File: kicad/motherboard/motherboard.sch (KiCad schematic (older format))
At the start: 21 parts, among them J1 DB37_Female, J10 DB37_Female, J11 DB37_Female, J12 Barrel_Jack, J13 TSR 1-2433, J2 DB37_Female, J3 DB37_Female, J4 DB37_Female, J5 DB37_Female, J6 DB25_Female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

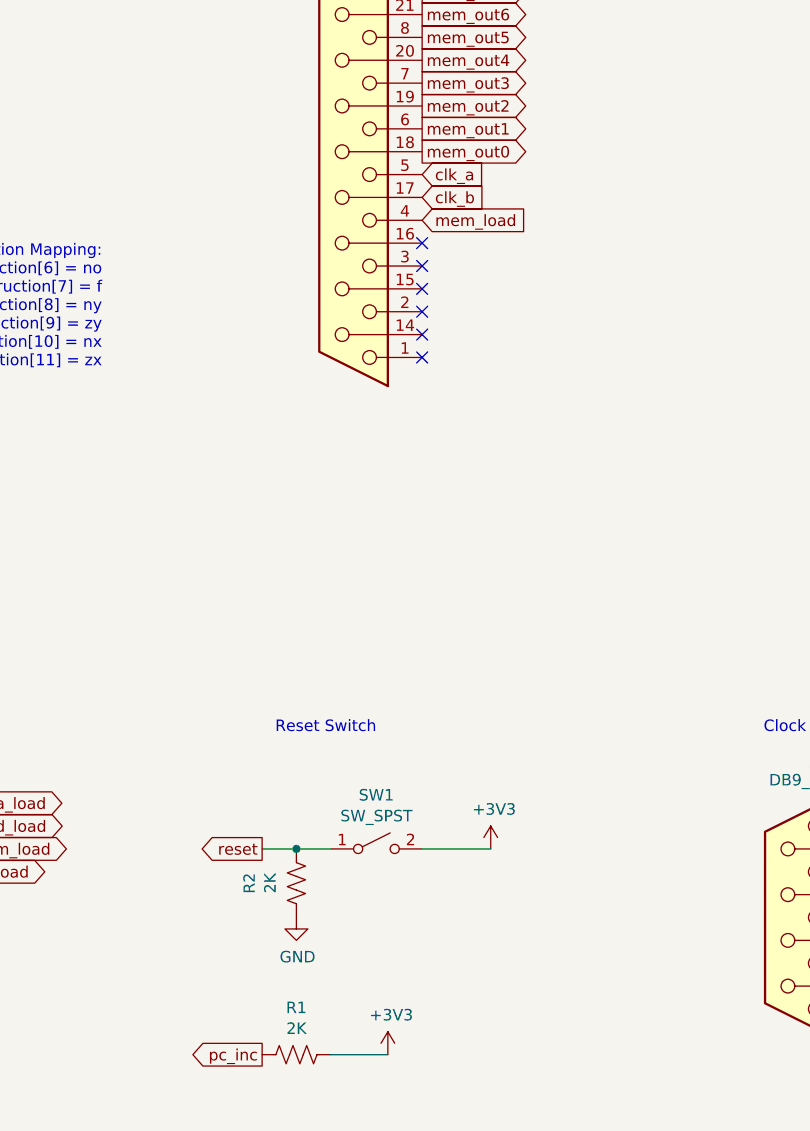
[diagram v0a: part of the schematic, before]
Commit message: Motherboard fully routed, PCB layout done
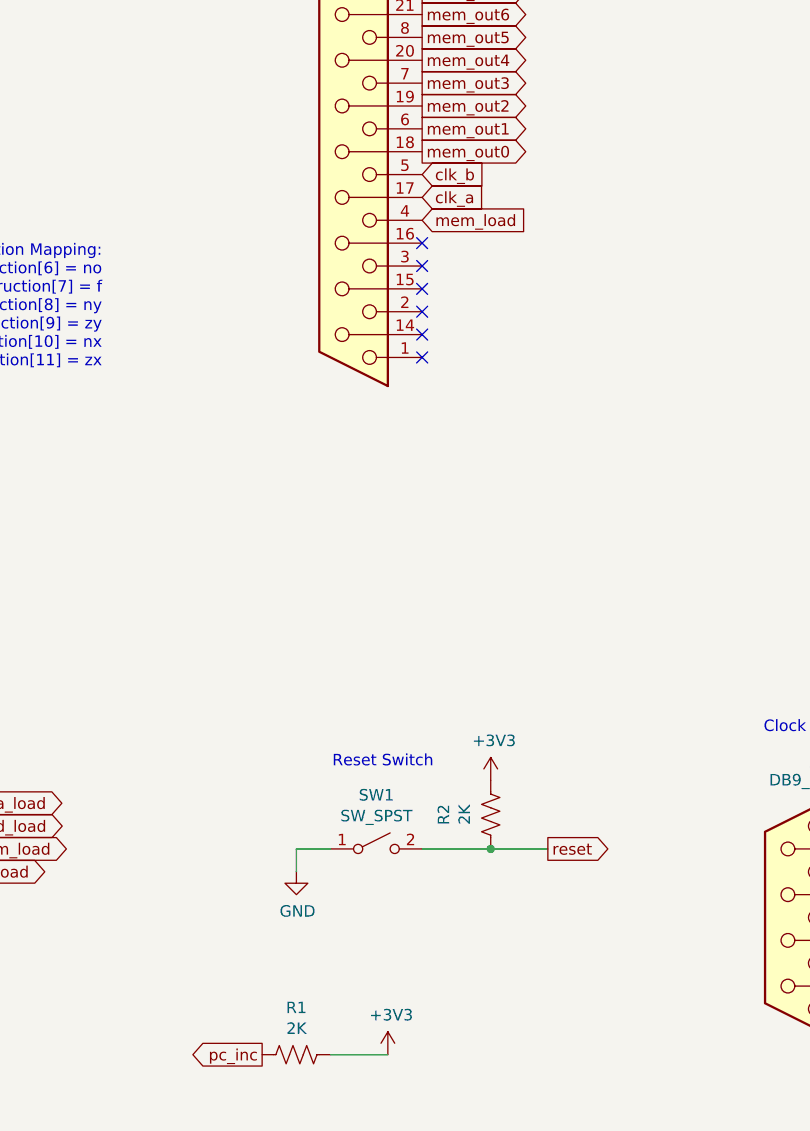
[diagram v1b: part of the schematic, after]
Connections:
- net +3V3: now also R2.1; no longer SW1.2 (B)
- net GND: now also SW1.1 (A); no longer R2.2
- net clk_a: now also J8.17 (P17); no longer J8.5
- net clk_b: now also J8.5; no longer J8.17 (P17)
- net reset: now also R2.2, SW1.2 (B); no longer R2.1, SW1.1 (A)
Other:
- moved on the sheet: R2
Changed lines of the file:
@@
 	1    0    0    -1
 $EndComp
-Text GLabel 3850 9800 0    50   Output ~ 0
+Text GLabel 5100 9800 2    50   Output ~ 0
 reset
 $Comp
 L Device:R_US R2
 U 1 1 5EA8D68F
-P 4000 9950
-F 0 "R2" V 3795 9950 50  0000 C CNN
-F 1 "2K" V 3886 9950 50  0000 C CNN
-F 2 "Resistor_SMD:R_1206_3216Metric" V 4040 9940 50  0001 C CNN
-F 3 "~" H 4000 9950 50  0001 C CNN
-	1    4000 9950
+P 4850 9650
+F 0 "R2" V 4645 9650 50  0000 C CNN
+F 1 "2K" V 4736 9650 50  0000 C CNN
+F 2 "Resistor_SMD:R_1206_3216Metric" V 4890 9640 50  0001 C CNN
+F 3 "~" H 4850 9650 50  0001 C CNN
+	1    4850 9650
 	1    0    0    -1
 $EndComp
@@
 L power:GND #PWR054
 U 1 1 5EA903DA
-P 4000 10100
-F 0 "#PWR054" H 4000 9850 50  0001 C CNN
-F 1 "GND" H 4005 9927 50  0000 C CNN
-F 2 "" H 4000 10100 50  0001 C CNN
-F 3 "" H 4000 10100 50  0001 C CNN
-	1    4000 10100
+P 4000 9900
+F 0 "#PWR054" H 4000 9650 50  0001 C CNN
+F 1 "GND" H 4005 9727 50  0000 C CNN
+F 2 "" H 4000 9900 50  0001 C CNN
+F 3 "" H 4000 9900 50  0001 C CNN
+	1    4000 9900
 	1    0    0    -1
 $EndComp
@@
 L power:+3V3 #PWR053
 U 1 1 5EA90EB0
-P 4850 9800
-F 0 "#PWR053" H 4850 9650 50  0001 C CNN
-F 1 "+3V3" H 4865 9973 50  0000 C CNN
-F 2 "" H 4850 9800 50  0001 C CNN
-F 3 "" H 4850 9800 50  0001 C CNN
-	1    4850 9800
-	1    0    0    -1
-$EndComp
-Wire Wire Line
-	3850 9800 4000 9800
-Connection ~ 4000 9800
+P 4850 9500
+F 0 "#PWR053" H 4850 9350 50  0001 C CNN
+F 1 "+3V3" H 4865 9673 50  0000 C CNN
+F 2 "" H 4850 9500 50  0001 C CNN
+F 3 "" H 4850 9500 50  0001 C CNN
+	1    4850 9500
+	1    0    0    -1
+$EndComp
 Wire Wire Line
 	4000 9800 4150 9800
@@
 Text Notes 9050 9300 2    50   ~ 0
 Power Input/Regulation
-Text Notes 4350 9300 2    50   ~ 0
+Text Notes 4600 9450 2    50   ~ 0
 Reset Switch
 Wire Wire Line
@@
 Text GLabel 4550 1100 2    50   Input ~ 0
 alu_out0
+Text GLabel 4550 6850 2    50   Input ~ 0
+clk_b
 Text GLabel 4550 6950 2    50   Input ~ 0
-clk_b
-Text GLabel 4550 6850 2    50   Input ~ 0
 clk_a
 Text GLabel 4550 7050 2    50   Input ~ 0
@@
 NoConn ~ 4550 7550
 NoConn ~ 4550 7650
+Wire Wire Line
+	4850 9800 5100 9800
+Connection ~ 4850 9800
+Wire Wire Line
+	4000 9800 4000 9900
 $EndSCHEMATC

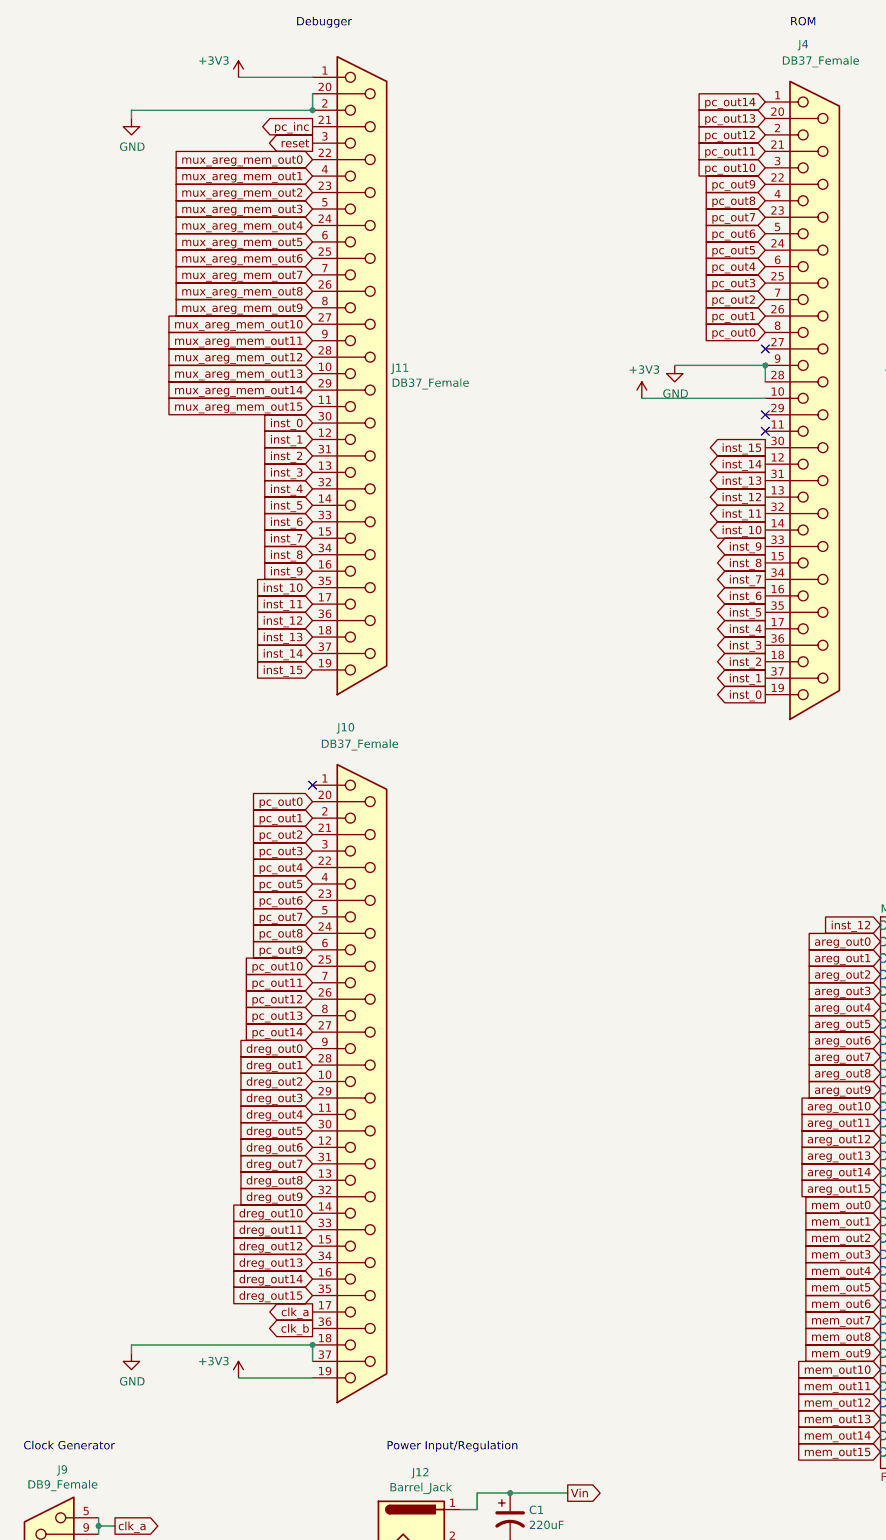
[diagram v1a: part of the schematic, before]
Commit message: Rom (#3)
* Updated motherboard with ROM OE,WE, and additional address pins

* ROM schematic, layout, routing complete.
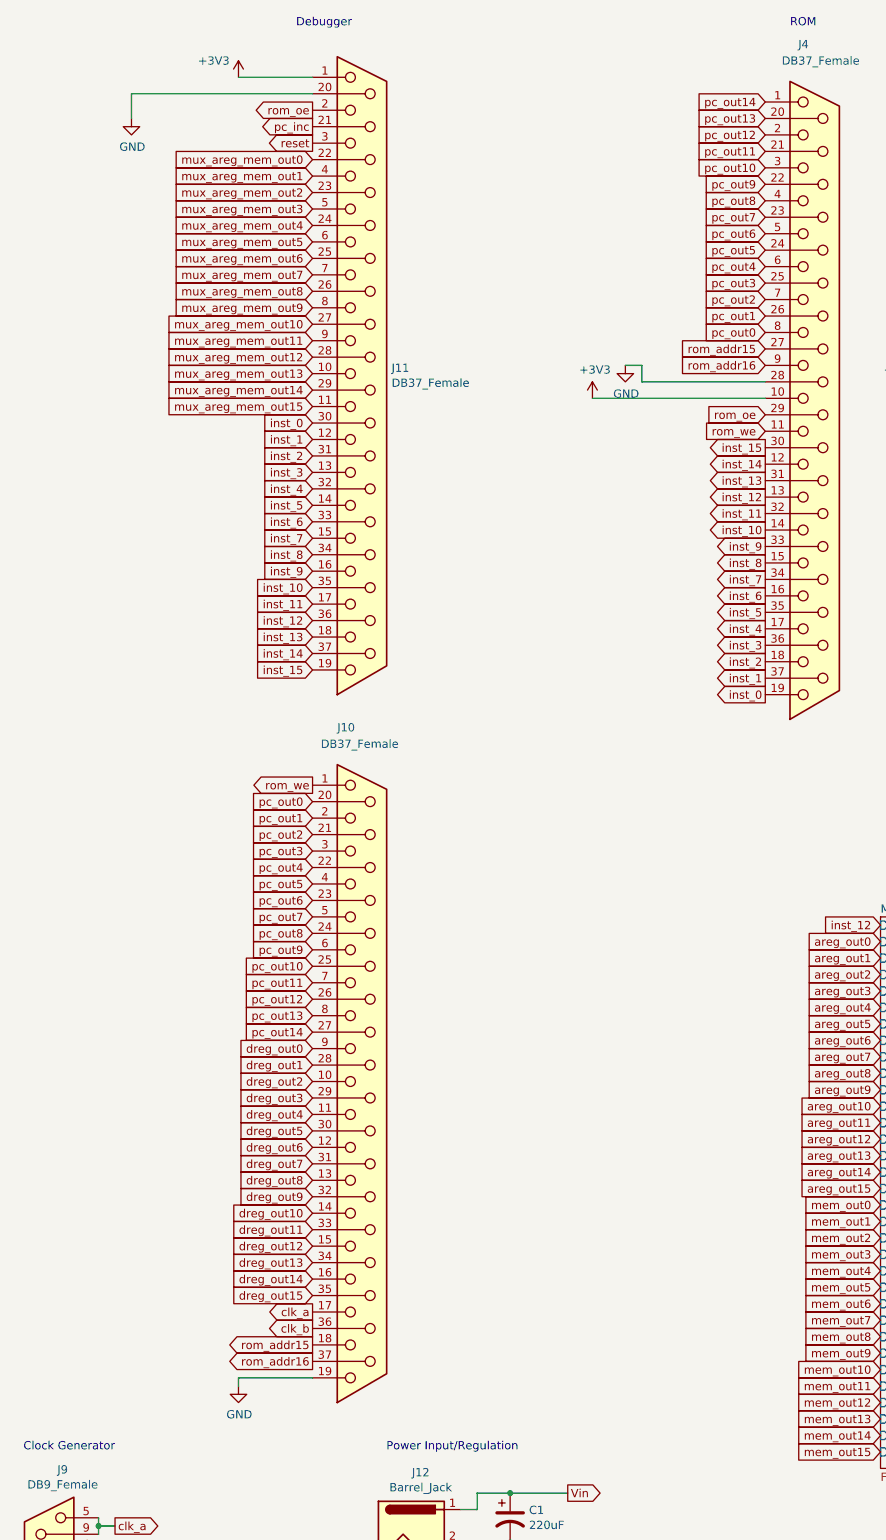
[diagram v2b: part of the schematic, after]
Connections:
- net +3V3: no longer J10.19
- net GND: now also J10.19; no longer J10.18, J10.37, J11.2, J4.9
- net rom_we: now reaches J10.1
- net rom_we: now also J4.11
- net rom_addr15: now reaches J4.27
- net rom_addr15: now also J10.18
- net rom_oe: now reaches J4.29
- net rom_oe: now also J11.2
- new net rom_addr16: J10.37, J4.9
- no-connect marks 12 -> 8
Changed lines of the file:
@@
 L power:GND #PWR08
 U 1 1 5E9B7F66
-P 10000 2700
-F 0 "#PWR08" H 10000 2450 50  0001 C CNN
-F 1 "GND" H 10005 2527 50  0000 C CNN
-F 2 "" H 10000 2700 50  0001 C CNN
-F 3 "" H 10000 2700 50  0001 C CNN
-	1    10000 2700
+P 9700 2700
+F 0 "#PWR08" H 9700 2450 50  0001 C CNN
+F 1 "GND" H 9705 2527 50  0000 C CNN
+F 2 "" H 9700 2700 50  0001 C CNN
+F 3 "" H 9700 2700 50  0001 C CNN
+	1    9700 2700
 	1    0    0    -1
 $EndComp
@@
 L power:+3V3 #PWR07
 U 1 1 5E9B7F6C
-P 9800 2900
-F 0 "#PWR07" H 9800 2750 50  0001 C CNN
-F 1 "+3V3" H 9815 3073 50  0000 C CNN
-F 2 "" H 9800 2900 50  0001 C CNN
-F 3 "" H 9800 2900 50  0001 C CNN
-	1    9800 2900
-	1    0    0    -1
-$EndComp
-Wire Wire Line
-	10000 2700 10550 2700
-Wire Wire Line
-	10550 2900 9800 2900
-Connection ~ 10550 2700
-Wire Wire Line
-	10550 2700 10550 2800
-NoConn ~ 10550 3000
-NoConn ~ 10550 3100
+P 9500 2900
+F 0 "#PWR07" H 9500 2750 50  0001 C CNN
+F 1 "+3V3" H 9515 3073 50  0000 C CNN
+F 2 "" H 9500 2900 50  0001 C CNN
+F 3 "" H 9500 2900 50  0001 C CNN
+	1    9500 2900
+	1    0    0    -1
+$EndComp
 $Comp
 L Connector:DB37_Female J5
@@
 clk_b
 Wire Wire Line
-	7800 8750 7800 8650
-Wire Wire Line
-	7800 8650 6700 8650
-Wire Wire Line
-	6700 8650 6700 8700
-Connection ~ 7800 8650
+	7350 8850 7350 8900
 $Comp
 L power:GND #PWR049
 U 1 1 5E99A741
-P 6700 8700
-F 0 "#PWR049" H 6700 8450 50  0001 C CNN
-F 1 "GND" H 6705 8527 50  0000 C CNN
-F 2 "" H 6700 8700 50  0001 C CNN
-F 3 "" H 6700 8700 50  0001 C CNN
-	1    6700 8700
-	1    0    0    -1
-$EndComp
-Wire Wire Line
-	7800 8850 7350 8850
-$Comp
-L power:+3V3 #PWR050
-U 1 1 5E99BD1A
-P 7350 8850
-F 0 "#PWR050" H 7350 8700 50  0001 C CNN
-F 1 "+3V3" H 7200 8950 50  0000 C CNN
-F 2 "" H 7350 8850 50  0001 C CNN
-F 3 "" H 7350 8850 50  0001 C CNN
-	1    7350 8850
-	1    0    0    -1
-$EndComp
-Wire Wire Line
-	7800 1050 7800 1150
-Wire Wire Line
-	7800 1150 6700 1150
-Connection ~ 7800 1150
-Wire Wire Line
-	6700 1150 6700 1200
+P 7350 8900
+F 0 "#PWR049" H 7350 8650 50  0001 C CNN
+F 1 "GND" H 7355 8727 50  0000 C CNN
+F 2 "" H 7350 8900 50  0001 C CNN
+F 3 "" H 7350 8900 50  0001 C CNN
+	1    7350 8900
+	1    0    0    -1
+$EndComp
 $Comp
 L power:GND #PWR052
@@
 $EndComp
 NoConn ~ 1750 6900
-NoConn ~ 10550 2600
 $Comp
 L Device:CP1 C2
@@
 Text GLabel 7800 1350 0    50   Output ~ 0
 reset
-NoConn ~ 7800 5250
 NoConn ~ 4550 7150
 NoConn ~ 4550 7250
@@
 Wire Wire Line
 	4000 9800 4000 9900
+Text GLabel 10550 2600 0    50   Input ~ 0
+rom_addr15
+Wire Wire Line
+	9800 2800 9800 2700
+Wire Wire Line
+	9800 2700 9700 2700
+Wire Wire Line
+	9800 2800 10550 2800
+Wire Wire Line
+	9500 2900 10550 2900
+Text GLabel 10550 2700 0    50   Input ~ 0
+rom_addr16
+Text GLabel 10550 3000 0    50   Input ~ 0
+rom_oe
+Text GLabel 10550 3100 0    50   Input ~ 0
+rom_we
+Text GLabel 7800 1150 0    50   Output ~ 0
+rom_oe
+Text GLabel 7800 5250 0    50   Output ~ 0
+rom_we
+Text GLabel 7800 8650 0    50   Output ~ 0
+rom_addr15
+Text GLabel 7800 8750 0    50   Output ~ 0
+rom_addr16
+Wire Wire Line
+	7800 8850 7350 8850
+Wire Wire Line
+	7800 1050 6700 1050
+Wire Wire Line
+	6700 1050 6700 1200
 $EndSCHEMATC
